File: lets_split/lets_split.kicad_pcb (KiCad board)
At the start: 2 copper layers, 112 x 79 mm, 62 parts, among them J1 3PIN, J2 6PIN, J3 3PIN, SW1 SW_PUSH, SW10 SW_PUSH, SW11 SW_PUSH, SW12 SW_PUSH, SW13 SW_PUSH, SW14 SW_PUSH, SW15 SW_PUSH, SW16 SW_PUSH, SW17 SW_PUSH, SW18 SW_PUSH, SW19 SW_PUSH, SW2 SW_PUSH, SW20 SW_PUSH, SW21 SW_PUSH, SW22 SW_PUSH, SW23 SW_PUSH, SW24 SW_PUSH, SW3 SW_PUSH, SW4 SW_PUSH, SW5 SW_PUSH, SW6 SW_PUSH, SW7 SW_PUSH, SW8 SW_PUSH, SW9 SW_PUSH, U1 ProMicro, U2 HOLE, U3 HOLE, U4 HOLE, U5 HOLE

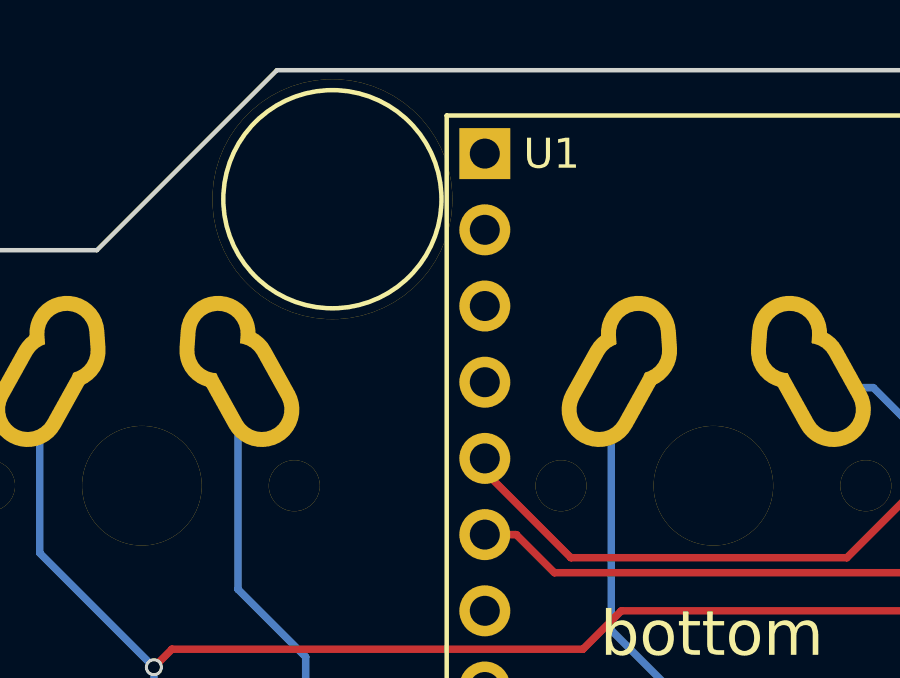
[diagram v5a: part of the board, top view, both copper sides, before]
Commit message: Add IO pad for RGB underglow
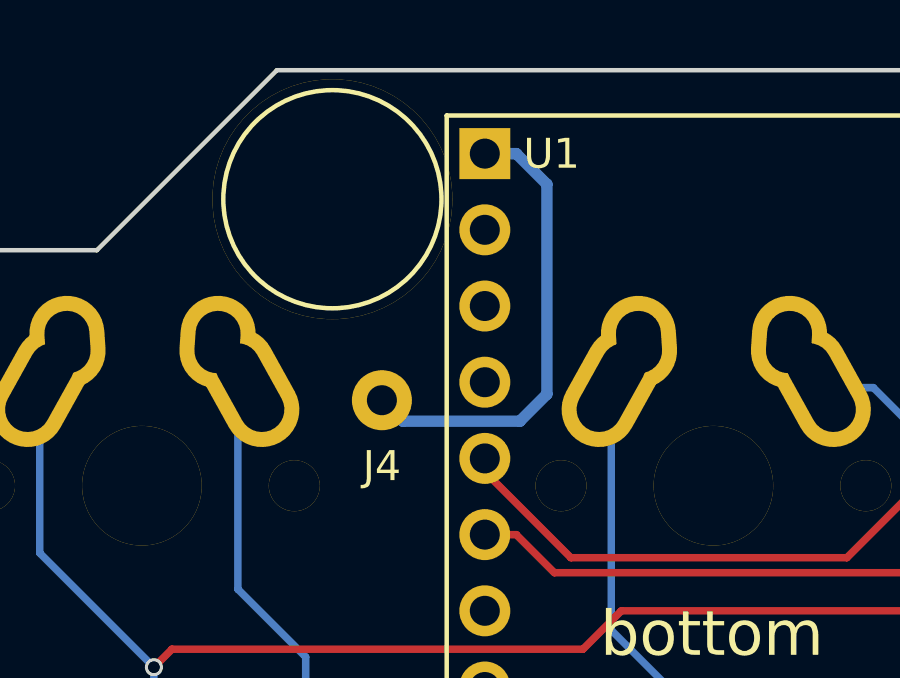
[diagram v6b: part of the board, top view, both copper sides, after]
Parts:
- added J4: CON1, local:CON1, F.Cu at (53.5, 44.0)
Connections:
- U1 pad 1: (no net) -> Net-(J4-Pad1)
- U1 pad 19: (no net) -> Net-(U1-Pad19)
- U1 pad 2: (no net) -> Net-(U1-Pad2)
- U1 pad 20: (no net) -> Net-(U1-Pad20)
- U1 pad 22: (no net) -> Net-(U1-Pad22)
- U1 pad 24: (no net) -> Net-(U1-Pad24)
- U1 pad 7: (no net) -> Net-(U1-Pad7)
- U1 pad 8: (no net) -> Net-(U1-Pad8)
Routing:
- net Net-(J4-Pad1): track 0.00 -> 15.7 mm
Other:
- board text added: "J4"
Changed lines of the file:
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@@
   (general
     (thickness 1.6)
-    (drawings 35)
-    (tracks 543)
+    (drawings 36)
+    (tracks 549)
     (zones 0)
-    (modules 62)
-    (nets 42)
+    (modules 63)
+    (nets 50)
   )
   (page A4)
@@
   )
   (setup
-    (last_trace_width 0.25)
+    (last_trace_width 0.38)
     (user_trace_width 0.25)
     (user_trace_width 0.38)
@@
   (net 40 col4)
   (net 41 col5)
+  (net 42 "Net-(J4-Pad1)")
+  (net 43 "Net-(U1-Pad24)")
+  (net 44 "Net-(U1-Pad22)")
+  (net 45 "Net-(U1-Pad20)")
+  (net 46 "Net-(U1-Pad19)")
+  (net 47 "Net-(U1-Pad8)")
+  (net 48 "Net-(U1-Pad7)")
+  (net 49 "Net-(U1-Pad2)")
   (net_class Default "This is the default net class."
     (clearance 0)
@@
     (add_net "Net-(J1-Pad2)")
     (add_net "Net-(J2-Pad4)")
+    (add_net "Net-(J4-Pad1)")
     (add_net "Net-(R1-Pad2)")
+    (add_net "Net-(U1-Pad19)")
+    (add_net "Net-(U1-Pad2)")
+    (add_net "Net-(U1-Pad20)")
+    (add_net "Net-(U1-Pad22)")
+    (add_net "Net-(U1-Pad24)")
+    (add_net "Net-(U1-Pad7)")
+    (add_net "Net-(U1-Pad8)")
     (add_net VCC)
     (add_net col0)
@@
       (effects (font (size 1.5 1.5) (thickness 0.3)))
     )
-    (pad 24 thru_hole circle (at -13.97 -7.62 270) (size 1.7 1.7) (drill 1) (layers *.Cu *.Mask))
+    (pad 24 thru_hole circle (at -13.97 -7.62 270) (size 1.7 1.7) (drill 1) (layers *.Cu *.Mask)
+      (net 43 "Net-(U1-Pad24)"))
     (pad 23 thru_hole circle (at -11.43 -7.62 270) (size 1.7 1.7) (drill 1) (layers *.Cu *.Mask)
       (net 29 GND))
-    (pad 22 thru_hole circle (at -8.89 -7.62 270) (size 1.7 1.7) (drill 1) (layers *.Cu *.Mask))
+    (pad 22 thru_hole circle (at -8.89 -7.62 270) (size 1.7 1.7) (drill 1) (layers *.Cu *.Mask)
+      (net 44 "Net-(U1-Pad22)"))
     (pad 21 thru_hole circle (at -6.35 -7.62 270) (size 1.7 1.7) (drill 1) (layers *.Cu *.Mask)
       (net 31 VCC))
-    (pad 20 thru_hole circle (at -3.81 -7.62 270) (size 1.7 1.7) (drill 1) (layers *.Cu *.Mask))
-    (pad 19 thru_hole circle (at -1.27 -7.62 270) (size 1.7 1.7) (drill 1) (layers *.Cu *.Mask))
+    (pad 20 thru_hole circle (at -3.81 -7.62 270) (size 1.7 1.7) (drill 1) (layers *.Cu *.Mask)
+      (net 45 "Net-(U1-Pad20)"))
+    (pad 19 thru_hole circle (at -1.27 -7.62 270) (size 1.7 1.7) (drill 1) (layers *.Cu *.Mask)
+      (net 46 "Net-(U1-Pad19)"))
     (pad 18 thru_hole circle (at 1.27 -7.62 270) (size 1.7 1.7) (drill 1) (layers *.Cu *.Mask)
       (net 36 col0))
@@
     (pad 9 thru_hole circle (at 6.35 7.62 270) (size 1.7 1.7) (drill 1) (layers *.Cu *.Mask)
       (net 2 row0))
-    (pad 8 thru_hole circle (at 3.81 7.62 270) (size 1.7 1.7) (drill 1) (layers *.Cu *.Mask))
-    (pad 7 thru_hole circle (at 1.27 7.62 270) (size 1.7 1.7) (drill 1) (layers *.Cu *.Mask))
+    (pad 8 thru_hole circle (at 3.81 7.62 270) (size 1.7 1.7) (drill 1) (layers *.Cu *.Mask)
+      (net 47 "Net-(U1-Pad8)"))
+    (pad 7 thru_hole circle (at 1.27 7.62 270) (size 1.7 1.7) (drill 1) (layers *.Cu *.Mask)
+      (net 48 "Net-(U1-Pad7)"))
     (pad 6 thru_hole circle (at -1.27 7.62 270) (size 1.7 1.7) (drill 1) (layers *.Cu *.Mask)
       (net 32 data))
@@
     (pad 3 thru_hole circle (at -8.89 7.62 270) (size 1.7 1.7) (drill 1) (layers *.Cu *.Mask)
       (net 29 GND))
-    (pad 2 thru_hole circle (at -11.43 7.62 270) (size 1.7 1.7) (drill 1) (layers *.Cu *.Mask))
-    (pad 1 thru_hole rect (at -13.97 7.62 270) (size 1.7 1.7) (drill 1) (layers *.Cu *.Mask))
+    (pad 2 thru_hole circle (at -11.43 7.62 270) (size 1.7 1.7) (drill 1) (layers *.Cu *.Mask)
+      (net 49 "Net-(U1-Pad2)"))
+    (pad 1 thru_hole rect (at -13.97 7.62 270) (size 1.7 1.7) (drill 1) (layers *.Cu *.Mask)
+      (net 42 "Net-(J4-Pad1)"))
   )
   (module local:RESISTOR (layer B.Cu)
@@
     (pad "" thru_hole circle (at -1.65 -0.7) (size 8 8) (drill 8) (layers *.Cu *.Mask F.SilkS))
   )
+  (module local:CON1 (layer F.Cu)
+    (at 53.5 44)
+    (fp_text reference J4 (at 0 2.2) (layer F.SilkS)
+      (effects (font (size 1 1) (thickness 0.15)))
+    )
+    (fp_text value CON1 (at 0 -1.7) (layer F.Fab) hide
+      (effects (font (size 1 1) (thickness 0.15)))
+    )
+    (pad 1 thru_hole circle (at 0 0) (size 2 2) (drill 1) (layers *.Cu *.Mask)
+      (net 42 "Net-(J4-Pad1)"))
+  )
+  (gr_text J4 (at 53.5 46.2) (layer B.SilkS)
+    (effects (font (size 1 1) (thickness 0.15)) (justify mirror))
+  )
   (gr_line (start 55.6641 34.5059) (end 73.4441 34.5059) (angle 90) (layer B.SilkS) (width 0.15))
   (gr_line (start 55.6641 64.9859) (end 55.6641 34.5059) (angle 90) (layer B.SilkS) (width 0.15))
@@
   (segment (start 140.6 70.9) (end 140.6 77.83) (width 0.25) (layer B.Cu) (net 41))
   (segment (start 137.345 67.645) (end 140.6 70.9) (width 0.25) (layer B.Cu) (net 41))
+  (segment (start 56.93 35.78) (end 57.98 35.78) (width 0.38) (layer B.Cu) (net 42) (status 400000))
+  (segment (start 58.1 44.7) (end 54.2 44.7) (width 0.38) (layer B.Cu) (net 42) (status 800000))
+  (segment (start 59 43.8) (end 58.1 44.7) (width 0.38) (layer B.Cu) (net 42))
+  (segment (start 59 36.8) (end 59 43.8) (width 0.38) (layer B.Cu) (net 42))
+  (segment (start 57.98 35.78) (end 59 36.8) (width 0.38) (layer B.Cu) (net 42))
+  (segment (start 54.2 44.7) (end 53.5 44) (width 0.38) (layer B.Cu) (net 42) (status C00000))
   (zone (net 29) (net_name GND) (layer F.Cu) (hatch edge 0.508)
     (connect_pads (clearance 0.508))

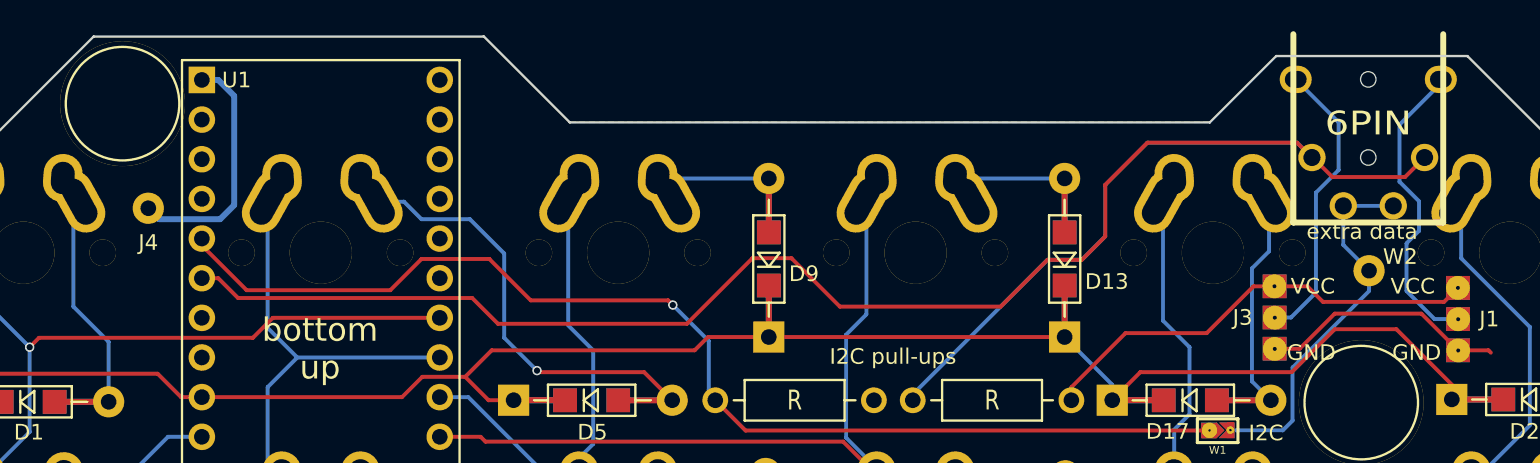
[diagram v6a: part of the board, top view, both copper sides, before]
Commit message: Add reset switch, changes outer shape of the board
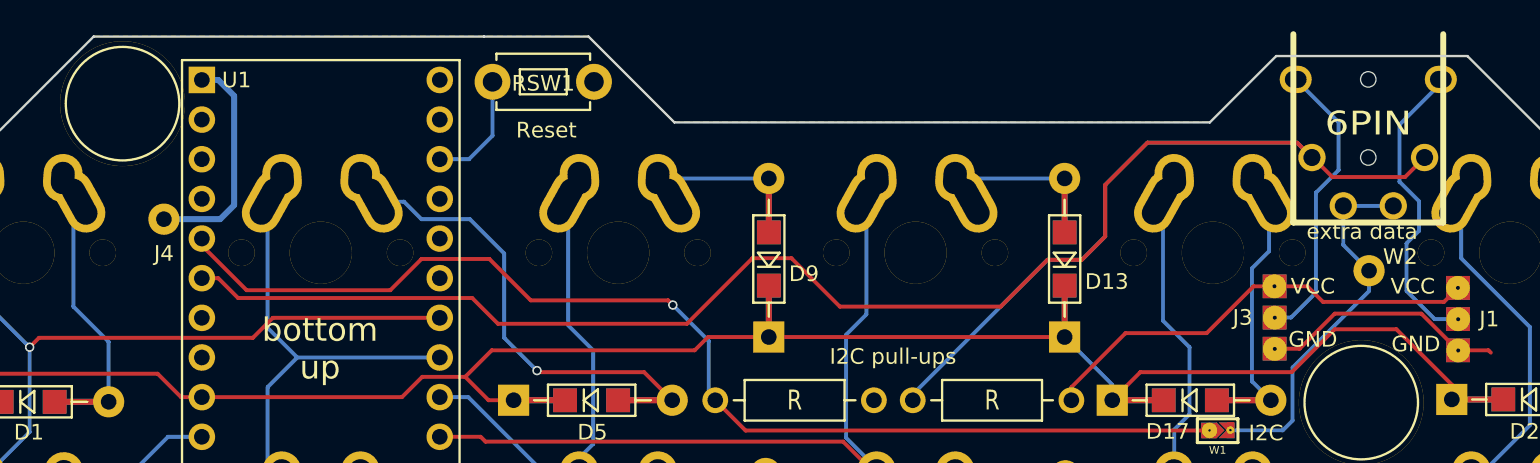
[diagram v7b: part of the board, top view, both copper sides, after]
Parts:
- added RSW1: SW_PUSH, local:SKHL, F.Cu at (78.8, 35.9)
- moved J4 1.22 mm to (54.5, 44.7)
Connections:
- U1 pad 19: Net-(U1-Pad19) -> (no net)
- U1 pad 2: Net-(U1-Pad2) -> (no net)
- U1 pad 20: Net-(U1-Pad20) -> (no net)
- U1 pad 24: Net-(U1-Pad24) -> (no net)
- U1 pad 7: Net-(U1-Pad7) -> (no net)
- U1 pad 8: Net-(U1-Pad8) -> (no net)
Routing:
- net Net-(RSW1-Pad1): track 0.00 -> 7.46 mm
- net Net-(J4-Pad1): track 15.7 -> 14.4 mm
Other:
- outline, holes or cut-outs redrawn
- board text added: "Reset"

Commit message: Rearrange schematic
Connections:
- net Net-(R1-Pad2) renamed I2C_SDA
